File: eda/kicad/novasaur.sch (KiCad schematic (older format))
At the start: 29 parts, among them U1 74F86, U10 74F574, U11 74F574, U12 PAL16R4, U2 74F32, U3 74F08, U4 74F139, U5 74F139, U6 74F157, U7 74F175, U8 74F574, U9 74F138, X1 33M

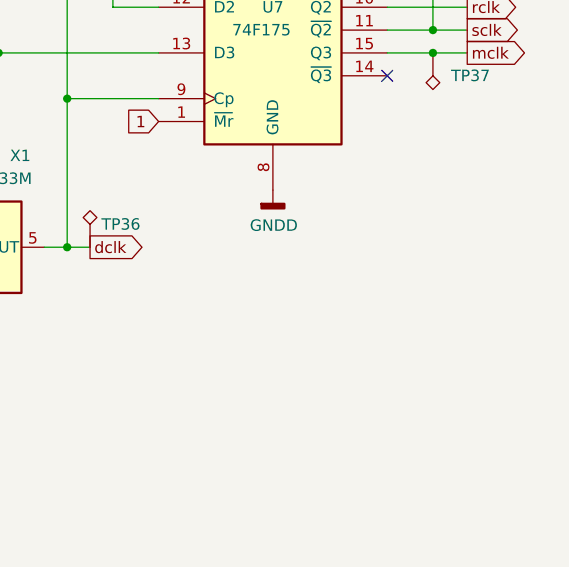
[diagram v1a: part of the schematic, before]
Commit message: fix video timing debug and finish video modes
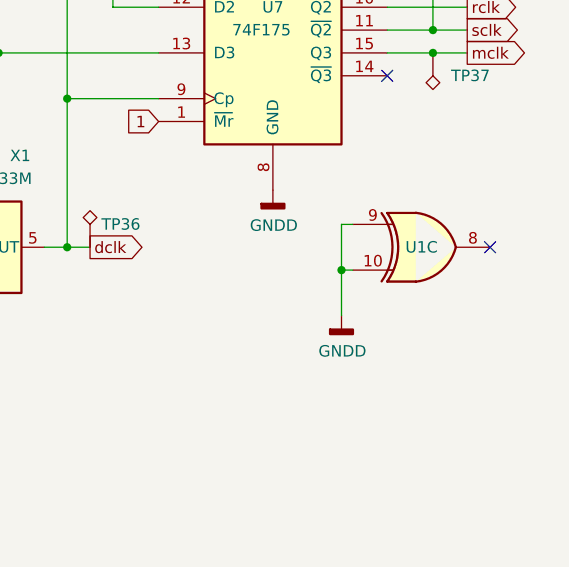
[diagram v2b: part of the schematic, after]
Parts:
- added unit 3 of U1
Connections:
- net GNDD: now also U1.10, U1.9
- no-connect marks 7 -> 8
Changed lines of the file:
@@
 Sheet 1 4
 Title "Novasaur Retrocomputer"
-Date "2020-08-20"
+Date "2020-09-10"
 Rev "1.7"
 Comp ""
@@
 	1    0    0    -1
 $EndComp
+$Comp
+L 74xx:74LS86 U1
+U 3 1 5F83F460
+P 9450 5500
+AR Path="/5F83F460" Ref="U1"  Part="3"
+AR Path="/5DA1E9BD/5F83F460" Ref="U?"  Part="3"
+F 0 "U1" H 9450 5500 50  0000 C CNN
+F 1 "74F86" H 9450 5734 50  0001 C CNN
+F 2 "Package_DIP:DIP-14_W7.62mm_LongPads" H 9450 5500 50  0001 C CNN
+F 3 "74xx/74ls86.pdf" H 9450 5500 50  0001 C CNN
+	3    9450 5500
+	1    0    0    -1
+$EndComp
+Wire Wire Line
+	9150 5400 9100 5400
+Wire Wire Line
+	9100 5400 9100 5600
+Wire Wire Line
+	9100 5600 9150 5600
+$Comp
+L power:GNDD #PWR?
+U 1 1 5F84F512
+P 9100 5800
+AR Path="/5CDEEC9F/5F84F512" Ref="#PWR?"  Part="1"
+AR Path="/5DAA5CD8/5F84F512" Ref="#PWR?"  Part="1"
+AR Path="/5F84F512" Ref="#PWR0203"  Part="1"
+F 0 "#PWR0203" H 9100 5550 50  0001 C CNN
+F 1 "GNDD" H 9104 5645 50  0000 C CNN
+F 2 "" H 9100 5800 50  0001 C CNN
+F 3 "" H 9100 5800 50  0001 C CNN
+	1    9100 5800
+	1    0    0    -1
+$EndComp
+Wire Wire Line
+	9100 5600 9100 5800
+Connection ~ 9100 5600
+NoConn ~ 9750 5500
 Wire Bus Line
 	4450 5100 4450 6750

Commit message: Fix audio Updates to make audio work after testing
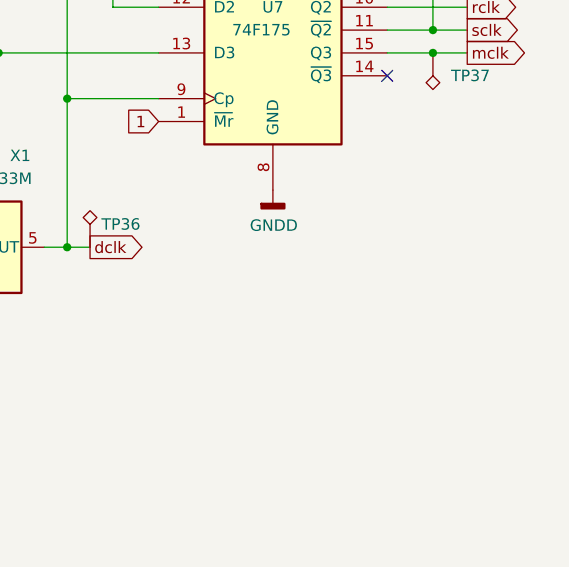
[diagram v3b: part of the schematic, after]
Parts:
- removed unit 3 of U1
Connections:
- no-connect marks 8 -> 7
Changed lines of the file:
@@
 	1    0    0    -1
 $EndComp
-$Comp
-L 74xx:74LS86 U1
-U 3 1 5F83F460
-P 9450 5500
-AR Path="/5F83F460" Ref="U1"  Part="3"
-AR Path="/5DA1E9BD/5F83F460" Ref="U?"  Part="3"
-F 0 "U1" H 9450 5500 50  0000 C CNN
-F 1 "74F86" H 9450 5734 50  0001 C CNN
-F 2 "Package_DIP:DIP-14_W7.62mm_LongPads" H 9450 5500 50  0001 C CNN
-F 3 "74xx/74ls86.pdf" H 9450 5500 50  0001 C CNN
-	3    9450 5500
-	1    0    0    -1
-$EndComp
-Wire Wire Line
-	9150 5400 9100 5400
-Wire Wire Line
-	9100 5400 9100 5600
-Wire Wire Line
-	9100 5600 9150 5600
-$Comp
-L power:GNDD #PWR?
-U 1 1 5F84F512
-P 9100 5800
-AR Path="/5CDEEC9F/5F84F512" Ref="#PWR?"  Part="1"
-AR Path="/5DAA5CD8/5F84F512" Ref="#PWR?"  Part="1"
-AR Path="/5F84F512" Ref="#PWR0203"  Part="1"
-F 0 "#PWR0203" H 9100 5550 50  0001 C CNN
-F 1 "GNDD" H 9104 5645 50  0000 C CNN
-F 2 "" H 9100 5800 50  0001 C CNN
-F 3 "" H 9100 5800 50  0001 C CNN
-	1    9100 5800
-	1    0    0    -1
-$EndComp
-Wire Wire Line
-	9100 5600 9100 5800
-Connection ~ 9100 5600
-NoConn ~ 9750 5500
 Wire Bus Line
 	4450 5100 4450 6750

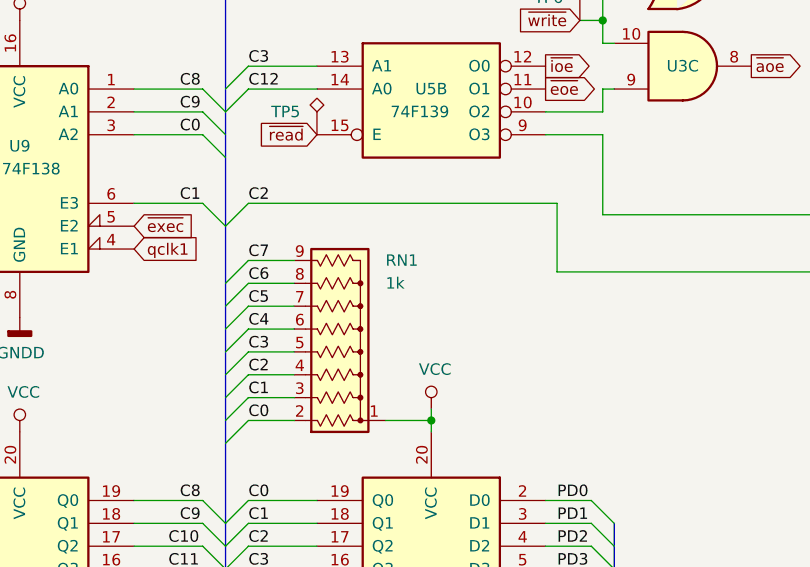
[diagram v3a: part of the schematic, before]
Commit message: audio muting and updated filter/inverting amplifier
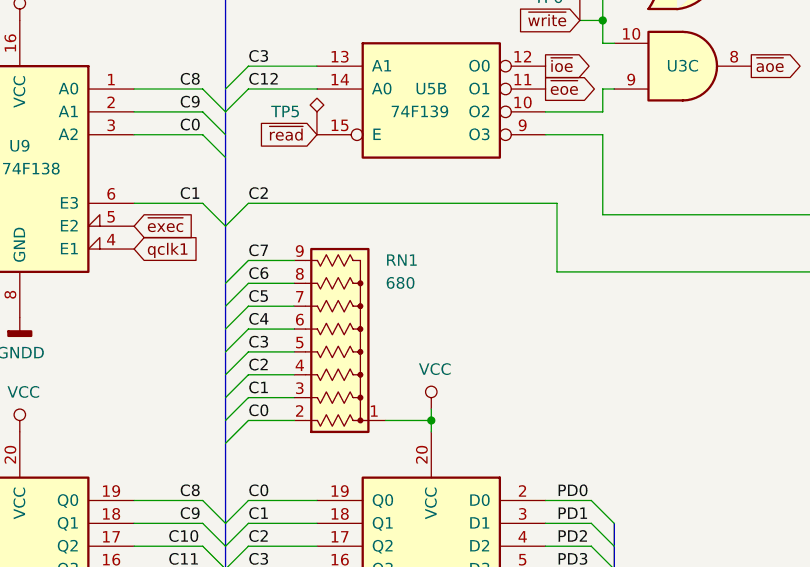
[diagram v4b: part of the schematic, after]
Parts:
- RN1: value 1k -> 680
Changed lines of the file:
@@
 Sheet 1 4
 Title "Novasaur Retrocomputer"
-Date "2020-09-10"
+Date "2020-10-01"
 Rev "1.7"
 Comp ""
@@
 AR Path="/5DA1E820" Ref="RN1"  Part="1"
 F 0 "RN1" V 3550 4450 50  0000 L CNN
-F 1 "1k" V 3450 4450 50  0000 L CNN
+F 1 "680" V 3450 4450 50  0000 L CNN
 F 2 "Resistor_THT:R_Array_SIP9" V 3725 4250 50  0001 C CNN
 F 3 "http://www.vishay.com/docs/31509/csc.pdf" H 3250 4250 50  0001 C CNN

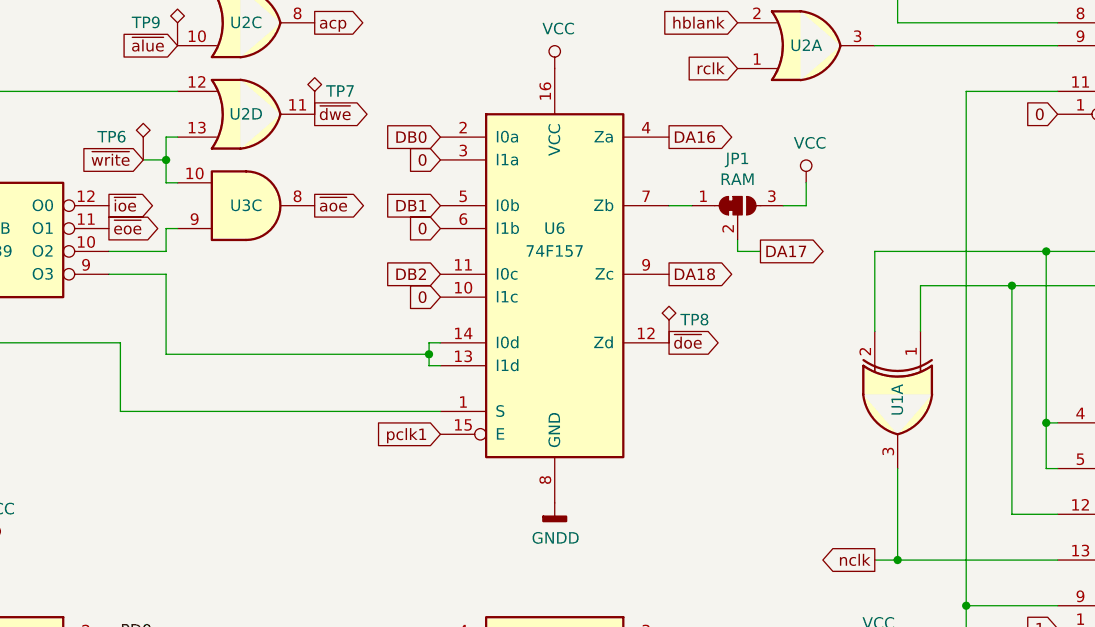
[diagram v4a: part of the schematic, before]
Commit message: rev 8 schematic stop FCP during blanking
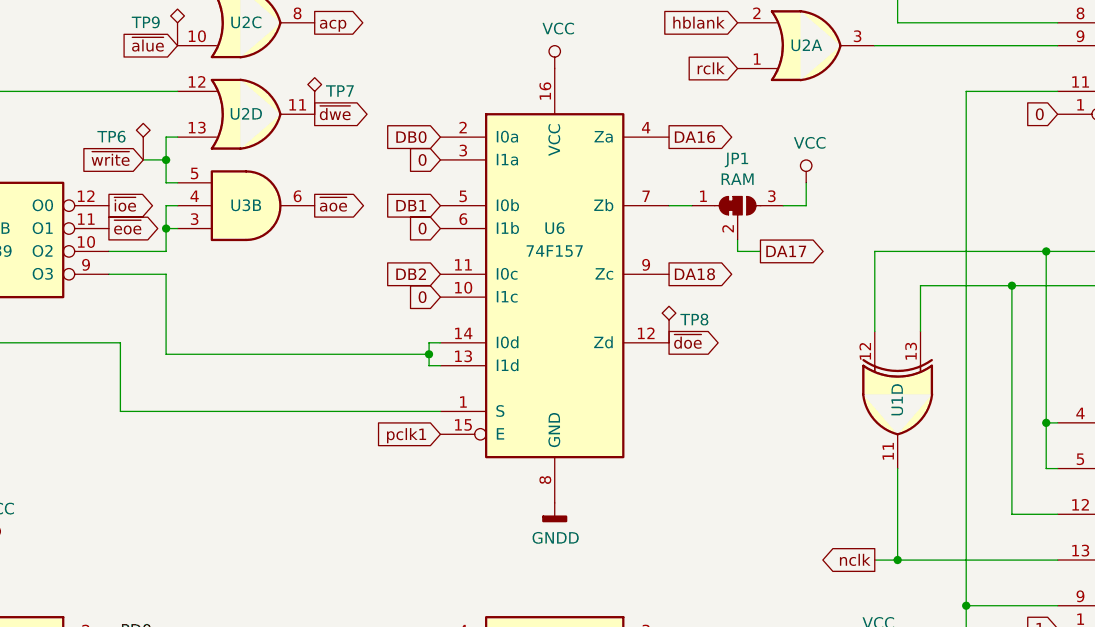
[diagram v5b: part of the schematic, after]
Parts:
- removed unit 1 of U1
- removed U3: 74F08, Package_DIP:DIP-14_W7.62mm_LongPads, symbol 74xx:74LS08
- added unit 4 of U1
- added U3: 74F11, Package_DIP:DIP-14_W7.62mm_LongPads, symbol 74xx:74LS11
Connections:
- net nclk: now also U1.11
- net pclk2: now also U1.13
- net sclk: now also U1.12
- net ~aoe: now also U3.6
- net ~write: now also U3.5
- net at U5.10 (O2): now also U3.3, U3.4
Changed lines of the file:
@@
 Sheet 1 4
 Title "Novasaur Retrocomputer"
-Date "2020-10-01"
-Rev "1.7"
+Date "2020-10-10"
+Rev "1.8"
 Comp ""
 Comment1 "(c) A J Hewitt 2020"
@@
 ~aoe
 $Comp
-L 74xx:74LS08 U?
-U 3 1 5DCA46DE
-P 4750 3100
-AR Path="/5CDEEC9F/5DCA46DE" Ref="U?"  Part="3"
-AR Path="/5DAA5CD8/5DCA46DE" Ref="U?"  Part="3"
-AR Path="/5DCA46DE" Ref="U3"  Part="3"
-AR Path="/5DA1E9BD/5DCA46DE" Ref="U?"  Part="3"
-F 0 "U3" H 4750 3100 50  0000 C CNN
-F 1 "74F08" H 4750 2900 50  0001 C CNN
-F 2 "Package_DIP:DIP-14_W7.62mm_LongPads" H 4750 3100 50  0001 C CNN
-F 3 "http://www.ti.com/lit/gpn/sn74LS08" H 4750 3100 50  0001 C CNN
-	3    4750 3100
-	1    0    0    1
-$EndComp
-$Comp
 L 74xx:74LS32 U?
 U 3 1 5E6A8202
@@
 Wire Wire Line
 	9300 4550 9500 4550
-$Comp
-L 74xx:74LS86 U1
-U 1 1 5D9EA8C5
-P 7600 3950
-F 0 "U1" H 7600 3950 50  0000 C CNN
-F 1 "74F86" H 7600 4184 50  0001 C CNN
-F 2 "Package_DIP:DIP-14_W7.62mm_LongPads" H 7600 3950 50  0001 C CNN
-F 3 "74xx/74ls86.pdf" H 7600 3950 50  0001 C CNN
-	1    7600 3950
-	0    1    1    0
-$EndComp
 Wire Wire Line
 	5550 3700 5600 3700
@@
 Wire Wire Line
 	7900 2600 8300 2600
-Wire Wire Line
-	4200 4000 5600 4000
 Wire Wire Line
 	4400 3750 5550 3750
@@
 	1    0    0    -1
 $EndComp
+Wire Wire Line
+	4200 4000 5600 4000
+$Comp
+L 74xx:74LS11 U?
+U 2 1 5FA4FFFA
+P 4750 3100
+AR Path="/5DA1E9BD/5FA4FFFA" Ref="U?"  Part="2"
+AR Path="/5FA4FFFA" Ref="U3"  Part="2"
+F 0 "U3" H 4750 3100 50  0000 C CNN
+F 1 "74F11" H 4750 3334 50  0001 C CNN
+F 2 "Package_DIP:DIP-14_W7.62mm_LongPads" H 4750 3100 50  0001 C CNN
+F 3 "http://www.ti.com/lit/gpn/sn74LS11" H 4750 3100 50  0001 C CNN
+	2    4750 3100
+	1    0    0    1
+$EndComp
+Wire Wire Line
+	4400 3200 4400 3100
+Wire Wire Line
+	4400 3100 4450 3100
+Connection ~ 4400 3200
+$Comp
+L 74xx:74LS86 U1
+U 4 1 5F86670E
+P 7600 3950
+AR Path="/5F86670E" Ref="U1"  Part="4"
+AR Path="/5DA1E9BD/5F86670E" Ref="U?"  Part="4"
+AR Path="/5DA1E9BA/5F86670E" Ref="U?"  Part="4"
+F 0 "U1" H 7600 3950 50  0000 C CNN
+F 1 "74F86" H 7600 4184 50  0001 C CNN
+F 2 "Package_DIP:DIP-14_W7.62mm_LongPads" H 7600 3950 50  0001 C CNN
+F 3 "74xx/74ls86.pdf" H 7600 3950 50  0001 C CNN
+	4    7600 3950
+	0    -1   1    0
+$EndComp
 Wire Bus Line

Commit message: rev 8 updates
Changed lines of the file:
@@
 Sheet 1 4
 Title "Novasaur Retrocomputer"
-Date "2020-10-10"
+Date "2020-10-15"
 Rev "1.8"
 Comp ""
@@
 AR Path="/5DA1E9BD/5E2B88BD" Ref="TP?"  Part="1"
 AR Path="/5DA1E9C0/5E2B88BD" Ref="TP?"  Part="1"
-F 0 "TP36" H 8050 5600 50  0000 L CNN
+F 0 "TP36" H 8050 5650 50  0000 L CNN
 F 1 "DCLK" H 7750 5650 50  0001 L CNN
 F 2 "TestPoint:TestPoint_THTPad_1.0x1.0mm_Drill0.5mm" H 8200 5500 50  0001 C CNN
@@
 AR Path="/5DA1E9BD/5EB702DB" Ref="TP?"  Part="1"
 AR Path="/5DA1E9C0/5EB702DB" Ref="TP?"  Part="1"
-F 0 "TP37" H 9250 4750 50  0000 L CNN
+F 0 "TP37" H 9250 4800 50  0000 L CNN
 F 1 "MCLK" H 9250 4800 50  0001 L CNN
 F 2 "TestPoint:TestPoint_Pad_1.0x1.0mm" H 9700 4650 50  0001 C CNN
